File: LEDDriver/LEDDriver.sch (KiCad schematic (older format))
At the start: 16 parts, among them CON1 36V DC Power, P1 En, P2 ToLED, P3 To5V Power, Q1 Q_PMOS_GDS

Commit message: lestarch: adding design files for combined design v2.0
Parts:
- removed P1: En, Pin_Headers:Pin_Header_Straight_1x01, symbol CONN_01X01
- removed P3: To5V Power, Pin_Headers:Pin_Header_Straight_1x02, symbol CONN_01X02
- added P1: FanOut, Pin_Headers:Pin_Header_Straight_1x02, symbol CONN_01X02
- added P3: TeensyConnector, Pin_Headers:Pin_Header_Straight_1x04, symbol CONN_01X04
- added Q2: Q_NMOS_GDS, footprints:TO-252-3, symbol Q_NMOS_GDS
- added R5, R6: R, Resistors_SMD:R_0402, symbol R
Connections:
- net GND: now also P3.2 (P2), Q2.3 (S)
- net at LM1.10 (CSN), R4.1: now also Q1.3 (S); no longer Q1.2 (D)
- net at LM1.4 (EN): now also P3.3 (P3)
- net at D1.1 (K), L1.1: now also Q1.2 (D); no longer Q1.3 (S)
- new net: P3.4 (P4), R5.1, R6.1
- new net: P1.2 (P2), Q2.2 (D)
- new net: Q2.1 (G), R6.2
- new net Regulator1/5VOut: P1.1 (P1), P3.1 (P1), R5.2
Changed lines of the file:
@@
 $Descr A4 11693 8268
 encoding utf-8
-Sheet 1 1
+Sheet 1 2
 Title ""
 Date ""
@@
 	1    0    0    -1
 $EndComp
-Wire Wire Line
-	5800 2100 5800 2050
-Wire Wire Line
-	5800 2050 6500 2050
-Wire Wire Line
-	5800 2300 5800 2350
-Wire Wire Line
-	5800 2350 5950 2350
-Connection ~ 5950 2050
 $Comp
 L GND #PWR01
@@
 	0    -1   -1   0
 $EndComp
-Wire Wire Line
-	6350 2350 6500 2350
 $Comp
 L VCC #PWR02
@@
 	0    1    1    0
 $EndComp
-Connection ~ 6350 2050
 $Comp
 L R R3
@@
 	-1   0    0    1
 $EndComp
-Wire Wire Line
-	5800 2400 6050 2400
-Wire Wire Line
-	6050 2400 6050 2300
-Wire Wire Line
-	6050 2300 6150 2300
-Wire Wire Line
-	6150 2300 6150 1850
-Connection ~ 6150 2050
-Wire Wire Line
-	6050 2600 6150 2600
-Wire Wire Line
-	6050 2600 6050 2500
-Wire Wire Line
-	6050 2500 5800 2500
-Wire Wire Line
-	6150 1850 5450 1850
-Wire Wire Line
-	5150 1850 4800 1850
-Wire Wire Line
-	4800 1850 4800 2100
-Wire Wire Line
-	4800 2100 4600 2100
 $Comp
 L GND #PWR03
@@
 	0    1    1    0
 $EndComp
-Wire Wire Line
-	4300 2100 4200 2100
 $Comp
 L GND #PWR04
@@
 	0    1    1    0
 $EndComp
-Wire Wire Line
-	4700 2600 4800 2600
 $Comp
 L C C1
@@
 	1    0    0    -1
 $EndComp
-Wire Wire Line
-	4150 2450 4500 2450
-Wire Wire Line
-	4500 2450 4500 2500
-Wire Wire Line
-	4500 2500 4800 2500
-Wire Wire Line
-	4350 2750 4750 2750
-Wire Wire Line
-	4750 2750 4750 2600
-Connection ~ 4750 2600
 $Comp
 L Q_PMOS_GDS Q1
@@
 F 3 "" H 6050 2800 60  0000 C CNN
 	1    6050 2800
-	1    0    0    -1
-$EndComp
-Connection ~ 6150 2600
-Wire Wire Line
-	5800 2600 5850 2600
-Wire Wire Line
-	5850 2600 5850 2800
+	1    0    0    1
+$EndComp
 $Comp
 L INDUCTOR L1
@@
 	0    -1   -1   0
 $EndComp
-Wire Wire Line
-	6500 3050 6450 3050
-Wire Wire Line
-	6150 3000 6150 3050
-Wire Wire Line
-	6150 3050 5600 3050
-Connection ~ 4350 2450
-Wire Wire Line
-	4150 2750 4150 3050
-Wire Wire Line
-	4150 3050 5000 3050
 $Comp
 L BARREL_JACK CON1
@@
 	-1   0    0    1
 $EndComp
-Wire Wire Line
-	4950 3350 4950 3050
-Connection ~ 4950 3050
-Wire Wire Line
-	4850 3250 4850 3350
-$Comp
-L CONN_01X02 P3
-U 1 1 5627469C
-P 5600 1350
-F 0 "P3" H 5600 1500 50  0000 C CNN
-F 1 "To5V Power" V 5700 1350 50  0000 C CNN
-F 2 "Pin_Headers:Pin_Header_Straight_1x02" H 5600 1350 60  0001 C CNN
-F 3 "" H 5600 1350 60  0000 C CNN
-	1    5600 1350
+$Comp
+L VCC #PWR09
+U 1 1 5627ABA1
+P 3300 1350
+F 0 "#PWR09" H 3300 1200 50  0001 C CNN
+F 1 "VCC" H 3300 1500 50  0000 C CNN
+F 2 "" H 3300 1350 60  0000 C CNN
+F 3 "" H 3300 1350 60  0000 C CNN
+	1    3300 1350
+	1    0    0    -1
+$EndComp
+$Comp
+L GND #PWR010
+U 1 1 5627ABD3
+P 3250 1750
+F 0 "#PWR010" H 3250 1500 50  0001 C CNN
+F 1 "GND" H 3250 1600 50  0000 C CNN
+F 2 "" H 3250 1750 60  0000 C CNN
+F 3 "" H 3250 1750 60  0000 C CNN
+	1    3250 1750
+	1    0    0    -1
+$EndComp
+$Comp
+L PWR_FLAG #FLG011
+U 1 1 5627AC05
+P 3150 1350
+F 0 "#FLG011" H 3150 1445 50  0001 C CNN
+F 1 "PWR_FLAG" H 3150 1530 50  0000 C CNN
+F 2 "" H 3150 1350 60  0000 C CNN
+F 3 "" H 3150 1350 60  0000 C CNN
+	1    3150 1350
 	0    -1   -1   0
 $EndComp
 $Comp
-L GND #PWR09
-U 1 1 56274723
-P 5650 1650
-F 0 "#PWR09" H 5650 1400 50  0001 C CNN
-F 1 "GND" H 5650 1500 50  0000 C CNN
-F 2 "" H 5650 1650 60  0000 C CNN
-F 3 "" H 5650 1650 60  0000 C CNN
-	1    5650 1650
-	1    0    0    -1
-$EndComp
-Wire Wire Line
-	5650 1650 5650 1550
-Wire Wire Line
-	5550 1550 5550 1850
-Connection ~ 5550 1850
-$Comp
-L CONN_01X01 P1
-U 1 1 56274A0B
-P 4150 2300
-F 0 "P1" H 4150 2400 50  0000 C CNN
-F 1 "En" V 4250 2300 50  0000 C CNN
-F 2 "Pin_Headers:Pin_Header_Straight_1x01" H 4150 2300 60  0001 C CNN
-F 3 "" H 4150 2300 60  0000 C CNN
-	1    4150 2300
-	-1   0    0    1
-$EndComp
-Wire Wire Line
-	4350 2300 4650 2300
-Wire Wire Line
-	4650 2300 4650 2400
-Wire Wire Line
-	4650 2400 4800 2400
-$Comp
-L VCC #PWR010
-U 1 1 5627ABA1
-P 3600 1400
-F 0 "#PWR010" H 3600 1250 50  0001 C CNN
-F 1 "VCC" H 3600 1550 50  0000 C CNN
-F 2 "" H 3600 1400 60  0000 C CNN
-F 3 "" H 3600 1400 60  0000 C CNN
-	1    3600 1400
-	1    0    0    -1
-$EndComp
-$Comp
-L GND #PWR011
-U 1 1 5627ABD3
-P 3600 1800
-F 0 "#PWR011" H 3600 1550 50  0001 C CNN
-F 1 "GND" H 3600 1650 50  0000 C CNN
-F 2 "" H 3600 1800 60  0000 C CNN
-F 3 "" H 3600 1800 60  0000 C CNN
-	1    3600 1800
-	1    0    0    -1
-$EndComp
-$Comp
 L PWR_FLAG #FLG012
-U 1 1 5627AC05
-P 3450 1400
-F 0 "#FLG012" H 3450 1495 50  0001 C CNN
-F 1 "PWR_FLAG" H 3450 1580 50  0000 C CNN
-F 2 "" H 3450 1400 60  0000 C CNN
-F 3 "" H 3450 1400 60  0000 C CNN
-	1    3450 1400
+U 1 1 5627AD59
+P 3150 1750
+F 0 "#FLG012" H 3150 1845 50  0001 C CNN
+F 1 "PWR_FLAG" H 3150 1930 50  0000 C CNN
+F 2 "" H 3150 1750 60  0000 C CNN
+F 3 "" H 3150 1750 60  0000 C CNN
+	1    3150 1750
 	0    -1   -1   0
 $EndComp
-Wire Wire Line
-	3600 1400 3450 1400
-$Comp
-L PWR_FLAG #FLG013
-U 1 1 5627AD59
-P 3450 1800
-F 0 "#FLG013" H 3450 1895 50  0001 C CNN
-F 1 "PWR_FLAG" H 3450 1980 50  0000 C CNN
-F 2 "" H 3450 1800 60  0000 C CNN
-F 3 "" H 3450 1800 60  0000 C CNN
-	1    3450 1800
-	0    -1   -1   0
-$EndComp
-Wire Wire Line
-	3450 1800 3600 1800
 NoConn ~ 4800 2300
 $Comp
@@
 	-1   0    0    1
 $EndComp
+$Comp
+L GND #PWR013
+U 1 1 57CE4B0C
+P 4850 1150
+F 0 "#PWR013" H 4850 900 50  0001 C CNN
+F 1 "GND" H 4850 1000 50  0000 C CNN
+F 2 "" H 4850 1150 50  0000 C CNN
+F 3 "" H 4850 1150 50  0000 C CNN
+	1    4850 1150
+	1    0    0    -1
+$EndComp
+$Comp
+L CONN_01X04 P3
+U 1 1 57CE4DDF
+P 4800 650
+F 0 "P3" H 4800 900 50  0000 C CNN
+F 1 "TeensyConnector" V 4900 650 50  0000 C CNN
+F 2 "Pin_Headers:Pin_Header_Straight_1x04" H 4800 650 50  0001 C CNN
+F 3 "" H 4800 650 50  0000 C CNN
+	1    4800 650
+	0    1    -1   0
+$EndComp
+$Comp
+L CONN_01X02 P1
+U 1 1 57CE52B5
+P 3950 650
+F 0 "P1" H 3950 800 50  0000 C CNN
+F 1 "FanOut" V 4050 650 50  0000 C CNN
+F 2 "Pin_Headers:Pin_Header_Straight_1x02" H 3950 650 50  0001 C CNN
+F 3 "" H 3950 650 50  0000 C CNN
+	1    3950 650
+	0    1    -1   0
+$EndComp
+$Comp
+L Q_NMOS_GDS Q2
+U 1 1 57CE561B
+P 4000 1300
+F 0 "Q2" H 4300 1350 50  0000 R CNN
+F 1 "Q_NMOS_GDS" H 4650 1250 50  0000 R CNN
+F 2 "footprints:TO-252-3" H 4200 1400 50  0001 C CNN
+F 3 "" H 4000 1300 50  0000 C CNN
+	1    4000 1300
+	-1   0    0    -1
+$EndComp
+$Comp
+L R R6
+U 1 1 57CE5FB3
+P 4400 1300
+F 0 "R6" V 4480 1300 50  0000 C CNN
+F 1 "R" V 4400 1300 50  0000 C CNN
+F 2 "Resistors_SMD:R_0402" V 4330 1300 50  0001 C CNN
+F 3 "" H 4400 1300 50  0000 C CNN
+	1    4400 1300
+	0    1    1    0
+$EndComp
+$Comp
+L R R5
+U 1 1 57CE62A6
+P 4550 1050
+F 0 "R5" V 4630 1050 50  0000 C CNN
+F 1 "R" V 4550 1050 50  0000 C CNN
+F 2 "Resistors_SMD:R_0402" V 4480 1050 50  0001 C CNN
+F 3 "" H 4550 1050 50  0000 C CNN
+	1    4550 1050
+	-1   0    0    1
+$EndComp
+$Sheet
+S 5100 800  550  300
+U 57CEDDA3
+F0 "Regulator1" 60
+F1 "5V1APowerSupply.sch" 60
+F2 "36VIn" I R 5650 900 60
+F3 "5VOut" I R 5650 1000 60
+$EndSheet
+Wire Wire Line
+	5800 2100 5800 2050
+Wire Wire Line
+	5800 2050 6500 2050
+Wire Wire Line
+	5800 2300 5800 2350
+Wire Wire Line
+	5800 2350 5950 2350
+Connection ~ 5950 2050
+Wire Wire Line
+	6350 2350 6500 2350
+Connection ~ 6350 2050
+Wire Wire Line
+	5800 2400 6050 2400
+Wire Wire Line
+	6050 2400 6050 2300
+Wire Wire Line
+	6050 2300 6150 2300
+Wire Wire Line
+	6150 2300 6150 900
+Connection ~ 6150 2050
+Wire Wire Line
+	6050 2600 6150 2600
+Wire Wire Line
+	6050 2600 6050 2500
+Wire Wire Line
+	6050 2500 5800 2500
+Wire Wire Line
+	6150 1850 5450 1850
+Wire Wire Line
+	5150 1850 4800 1850
+Wire Wire Line
+	4800 1850 4800 2100
+Wire Wire Line
+	4800 2100 4600 2100
+Wire Wire Line
+	4300 2100 4200 2100
+Wire Wire Line
+	4700 2600 4800 2600
+Wire Wire Line
+	4150 2450 4500 2450
+Wire Wire Line
+	4500 2450 4500 2500
+Wire Wire Line
+	4500 2500 4800 2500
+Wire Wire Line
+	4350 2750 4750 2750
+Wire Wire Line
+	4750 2750 4750 2600
+Connection ~ 4750 2600
+Connection ~ 6150 2600
+Wire Wire Line
+	5800 2600 5850 2600
+Wire Wire Line
+	5850 2600 5850 2800
+Wire Wire Line
+	6500 3050 6450 3050
+Wire Wire Line
+	6150 3000 6150 3050
+Wire Wire Line
+	6150 3050 5600 3050
+Connection ~ 4350 2450
+Wire Wire Line
+	4150 2750 4150 3050
+Wire Wire Line
+	4150 3050 5000 3050
+Wire Wire Line
+	4950 3350 4950 3050
+Connection ~ 4950 3050
+Wire Wire Line
+	4850 3250 4850 3350
+Wire Wire Line
+	3900 2300 4650 2300
+Wire Wire Line
+	4650 2300 4650 2400
+Wire Wire Line
+	4650 2400 4800 2400
 Wire Wire Line
 	6350 1150 6650 1150
@@
 Wire Wire Line
 	6650 1150 6650 1250
+Wire Wire Line
+	4850 850  4850 1150
+Wire Wire Line
+	3900 2300 3900 1900
+Wire Wire Line
+	3900 1900 4750 1900
+Wire Wire Line
+	4750 1900 4750 850
+Wire Wire Line
+	3900 850  3900 1100
+Wire Wire Line
+	4650 1300 4650 850
+Wire Wire Line
+	5650 1000 5700 1000
+Wire Wire Line
+	5700 1000 5700 1300
+Wire Wire Line
+	5700 1300 4950 1300
+Wire Wire Line
+	6150 900  5650 900
+Connection ~ 6150 1850
+Wire Wire Line
+	4000 850  4000 900
+Wire Wire Line
+	4950 1300 4950 850
+Connection ~ 4950 900
+Wire Wire Line
+	4550 1300 4650 1300
+Wire Wire Line
+	4550 1300 4550 1200
+Wire Wire Line
+	4000 900  4950 900
+Connection ~ 4550 900
+$Comp
+L GND #PWR014
+U 1 1 57CF08A9
+P 3900 1600
+F 0 "#PWR014" H 3900 1350 50  0001 C CNN
+F 1 "GND" H 3900 1450 50  0000 C CNN
+F 2 "" H 3900 1600 50  0000 C CNN
+F 3 "" H 3900 1600 50  0000 C CNN
+	1    3900 1600
+	1    0    0    -1
+$EndComp
+Wire Wire Line
+	3900 1500 3900 1600
+Wire Wire Line
+	4250 1300 4200 1300
+Wire Wire Line
+	3300 1350 3150 1350
+Wire Wire Line
+	3250 1750 3150 1750
 $EndSCHEMATC

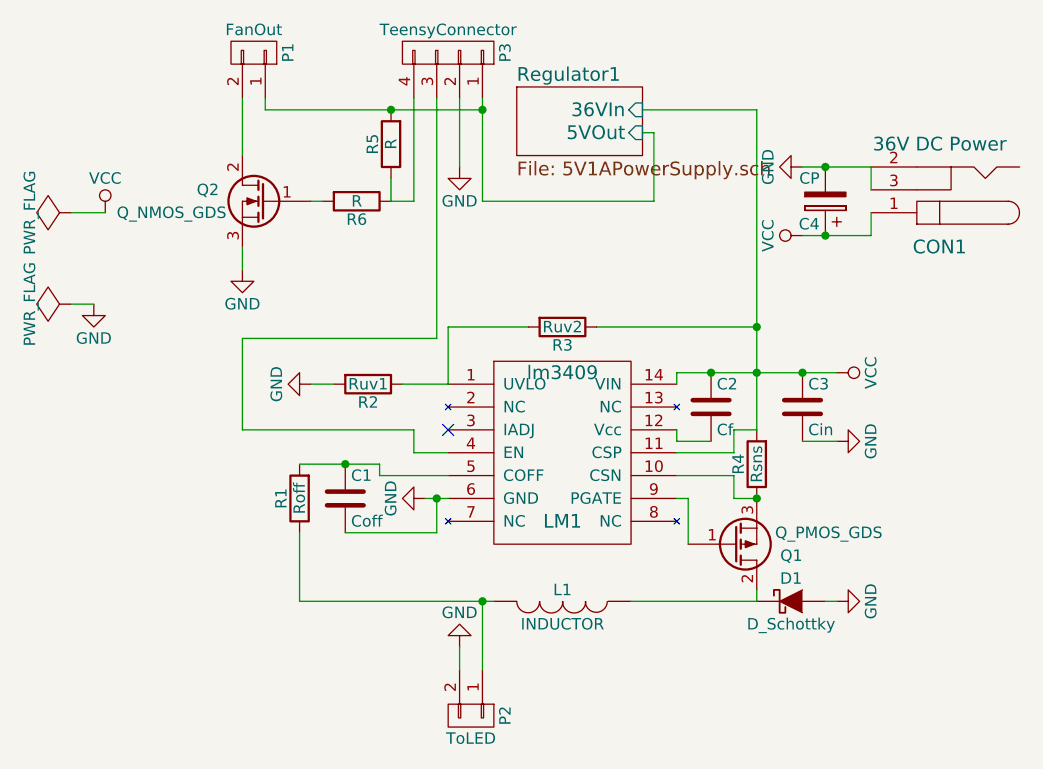
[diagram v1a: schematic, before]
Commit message: lestarch: changing resistors to pulldown resistors; adding pulldown to LED
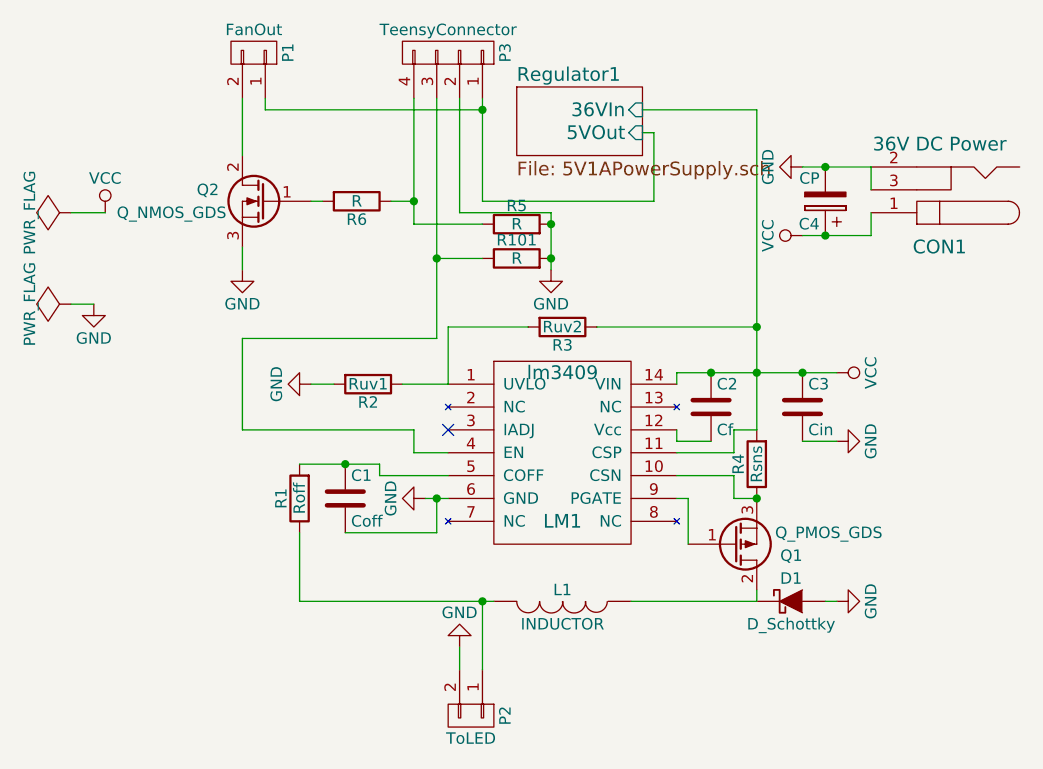
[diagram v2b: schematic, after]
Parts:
- added R101: R, Resistors_SMD:R_0402, symbol R
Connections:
- net GND: now also R5.2, R101.2
- net Regulator1/5VOut: no longer R5.2
- net at LM1.4 (EN), P3.3 (P3): now also R101.1
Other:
- moved on the sheet: R5
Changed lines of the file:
@@
 L GND #PWR013
 U 1 1 57CE4B0C
-P 4850 1150
-F 0 "#PWR013" H 4850 900 50  0001 C CNN
-F 1 "GND" H 4850 1000 50  0000 C CNN
-F 2 "" H 4850 1150 50  0000 C CNN
-F 3 "" H 4850 1150 50  0000 C CNN
-	1    4850 1150
+P 5250 1600
+F 0 "#PWR013" H 5250 1350 50  0001 C CNN
+F 1 "GND" H 5250 1450 50  0000 C CNN
+F 2 "" H 5250 1600 50  0000 C CNN
+F 3 "" H 5250 1600 50  0000 C CNN
+	1    5250 1600
 	1    0    0    -1
 $EndComp
@@
 L R R5
 U 1 1 57CE62A6
-P 4550 1050
-F 0 "R5" V 4630 1050 50  0000 C CNN
-F 1 "R" V 4550 1050 50  0000 C CNN
-F 2 "Resistors_SMD:R_0402" V 4480 1050 50  0001 C CNN
-F 3 "" H 4550 1050 50  0000 C CNN
-	1    4550 1050
-	-1   0    0    1
+P 5100 1400
+F 0 "R5" V 5180 1400 50  0000 C CNN
+F 1 "R" V 5100 1400 50  0000 C CNN
+F 2 "Resistors_SMD:R_0402" V 5030 1400 50  0001 C CNN
+F 3 "" H 5100 1400 50  0000 C CNN
+	1    5100 1400
+	0    -1   -1   0
 $EndComp
 $Sheet
@@
 	6650 1150 6650 1250
 Wire Wire Line
-	4850 850  4850 1150
-Wire Wire Line
 	3900 2300 3900 1900
 Wire Wire Line
 	3900 1900 4750 1900
 Wire Wire Line
-	4750 1900 4750 850
-Wire Wire Line
 	3900 850  3900 1100
-Wire Wire Line
-	4650 1300 4650 850
 Wire Wire Line
 	5650 1000 5700 1000
@@
 	4550 1300 4650 1300
 Wire Wire Line
-	4550 1300 4550 1200
-Wire Wire Line
 	4000 900  4950 900
-Connection ~ 4550 900
 $Comp
 L GND #PWR014
@@
 Wire Wire Line
 	3250 1750 3150 1750
+$Comp
+L R R101
+U 1 1 58025BA4
+P 5100 1550
+F 0 "R101" V 5180 1550 50  0000 C CNN
+F 1 "R" V 5100 1550 50  0000 C CNN
+F 2 "Resistors_SMD:R_0402" V 5030 1550 50  0001 C CNN
+F 3 "" H 5100 1550 50  0000 C CNN
+	1    5100 1550
+	0    -1   -1   0
+$EndComp
+Wire Wire Line
+	4750 1900 4750 850
+Wire Wire Line
+	4850 850  4850 1350
+Wire Wire Line
+	4850 1350 5250 1350
+Wire Wire Line
+	4650 850  4650 1400
+Wire Wire Line
+	5250 1350 5250 1600
+Connection ~ 5250 1400
+Connection ~ 5250 1550
+Wire Wire Line
+	4650 1400 4950 1400
+Connection ~ 4650 1300
+Wire Wire Line
+	4950 1550 4750 1550
+Connection ~ 4750 1550
 $EndSCHEMATC
